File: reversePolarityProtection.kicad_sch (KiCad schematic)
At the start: 4 parts, among them Q7 XPH3R114MC

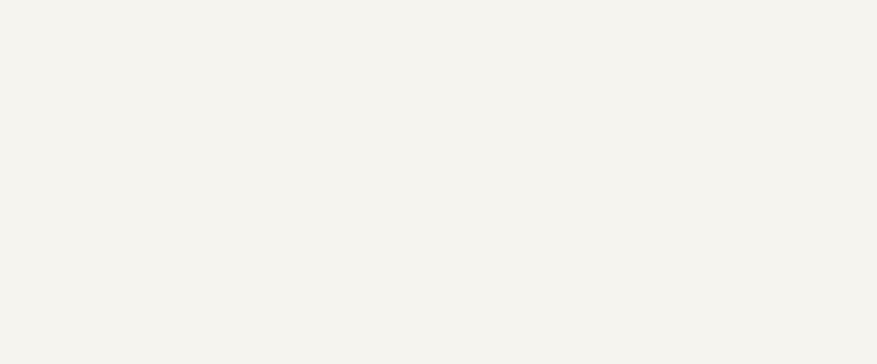
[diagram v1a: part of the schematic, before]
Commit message: Added Wakeup, supply, more pins on MCU
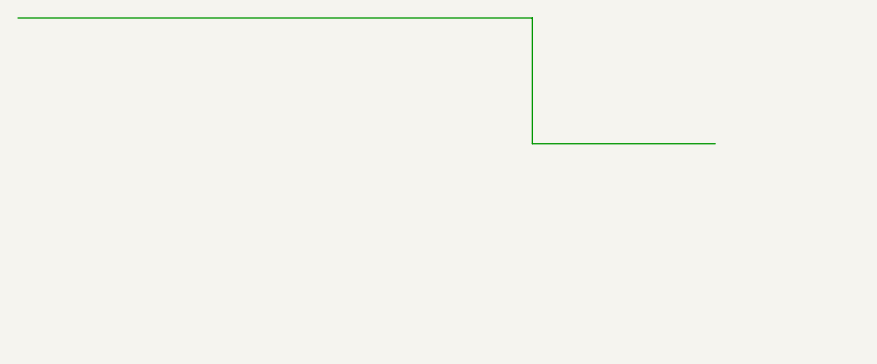
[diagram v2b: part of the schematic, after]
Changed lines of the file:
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@@
+	(wire
+		(pts
+			(xy 77.5462 14.0462) (xy 57.2262 14.0462)
+		)
+		(stroke
+			(width 0)
+			(type default)
+		)
+	)
 	(wire
 		(pts
@@
 	(wire
 		(pts
+			(xy 57.2262 14.0462) (xy 57.2262 0.0762)
+		)
+		(stroke
+			(width 0)
+			(type default)
+		)
+	)
+	(wire
+		(pts
 			(xy 154.94 90.17) (xy 154.94 96.52)
 		)
 		(stroke
+			(width 0)
+			(type default)
+		)
+	)
+	(wire
+		(pts
+			(xy 57.2262 0.0762) (xy 0.0762 0.0762)
+		)
+		(stroke

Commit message: Checked pinouts
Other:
- note added: "Checked ok"
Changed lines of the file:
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@@
 	(generator_version "10.0")
 	(paper "A4")
+	(text "Checked ok"
+		(exclude_from_sim no)
+		(at 199.39 173.482 0)
+		(effects
+			(font
+				(size 1.27 1.27)
+			)
+		)
+	)
 	(junction
 		(at 162.56 82.55)

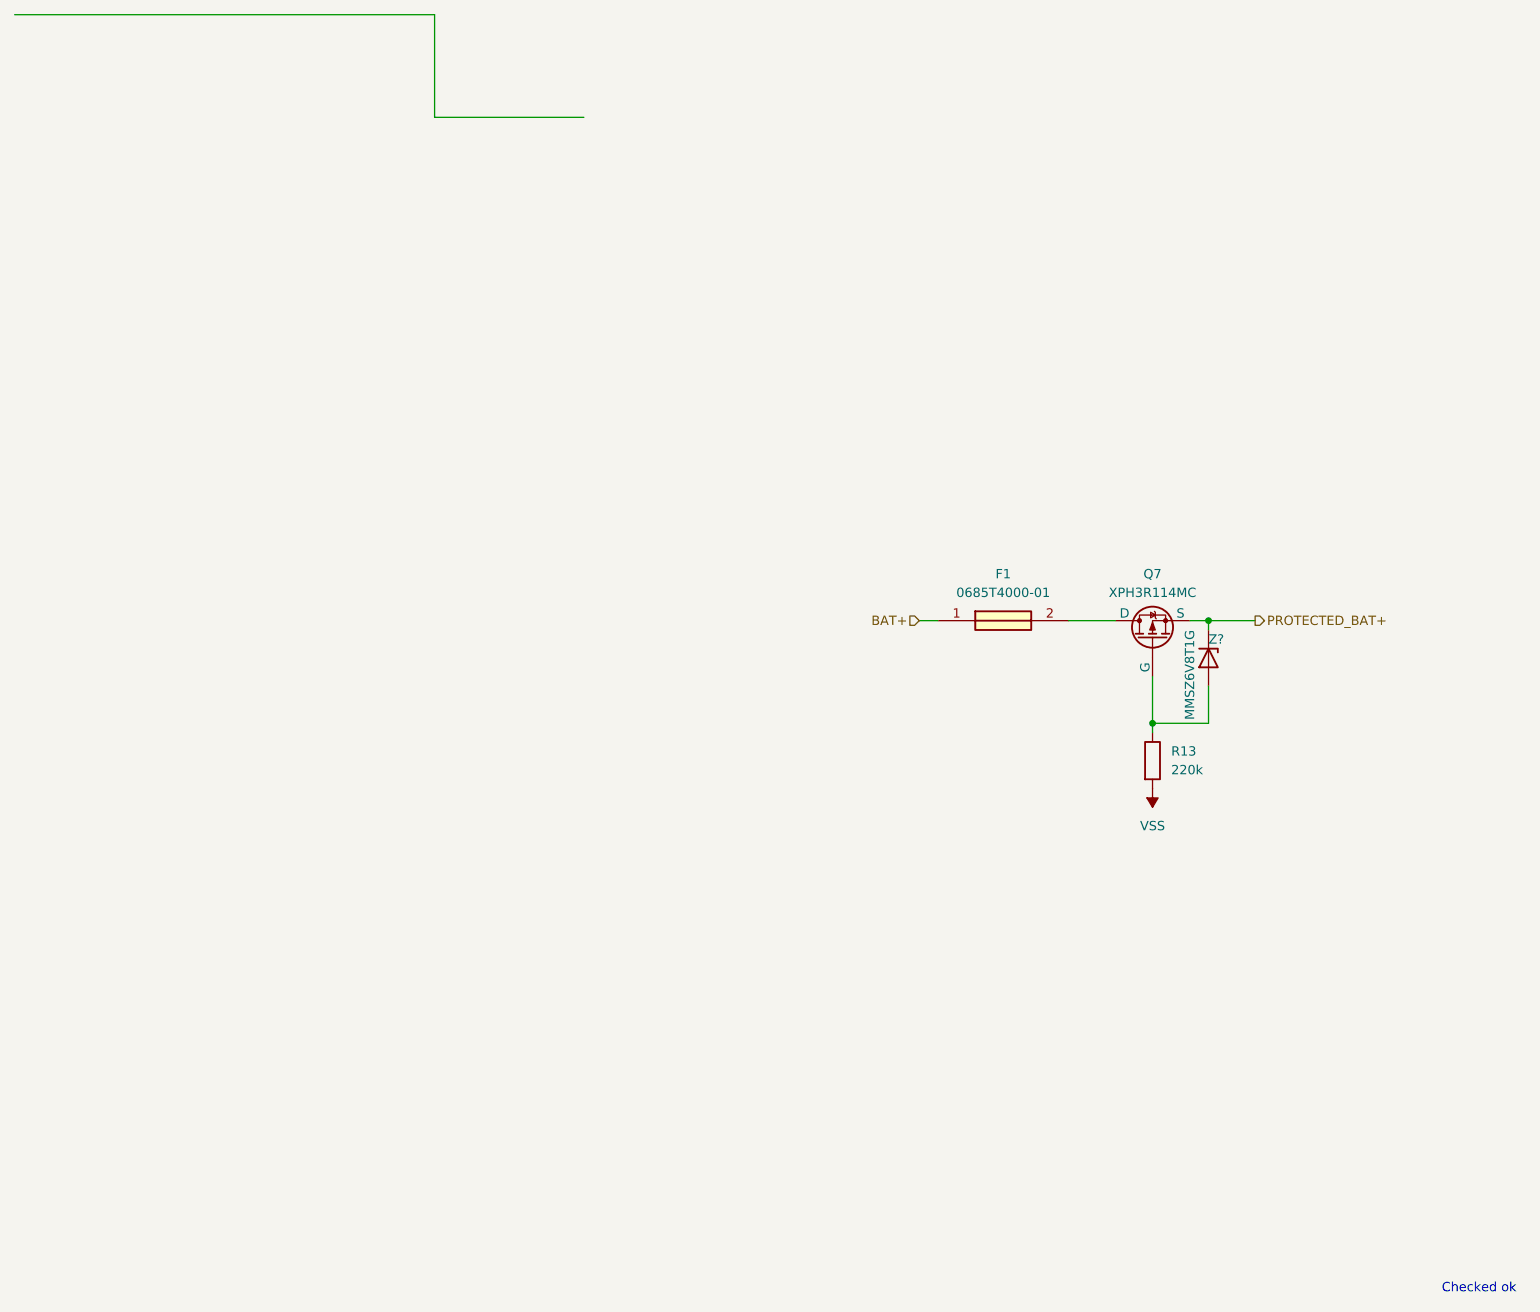
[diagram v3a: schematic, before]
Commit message: Review and update reversePolarityProtection schematic
- Annotate Zener Z? → Z1
- Replace fuse F1: 0685T4000-01 (4A Bel) → SF-1206HH25M-2 (25A Bourns),
  same 1206 footprint updated to Fuse:Fuse_1206_3216Metric
- Add TVS1 TPSMF4L20A (Littelfuse SOD-123FL, 20V standoff, 32.4V clamp,
  AEC-Q101) on BAT+ input rail for ISO 7637-2 load dump protection
- Add C1 4.7uF/50V X7R MLCC 1210 (Murata GRM32ER71H475KA88L) in parallel
  with TVS1 for high-frequency transient bypass, zero leakage in sleep
- Fix Q7 (XPH3R114MC) datasheet link: was ngspice URL, now Toshiba datasheet
- Remove three orphaned stray wires near schematic origin (0,0)

https://claude.ai/code/session_01Q9peTQ2YtBwmEgSRVprrxD
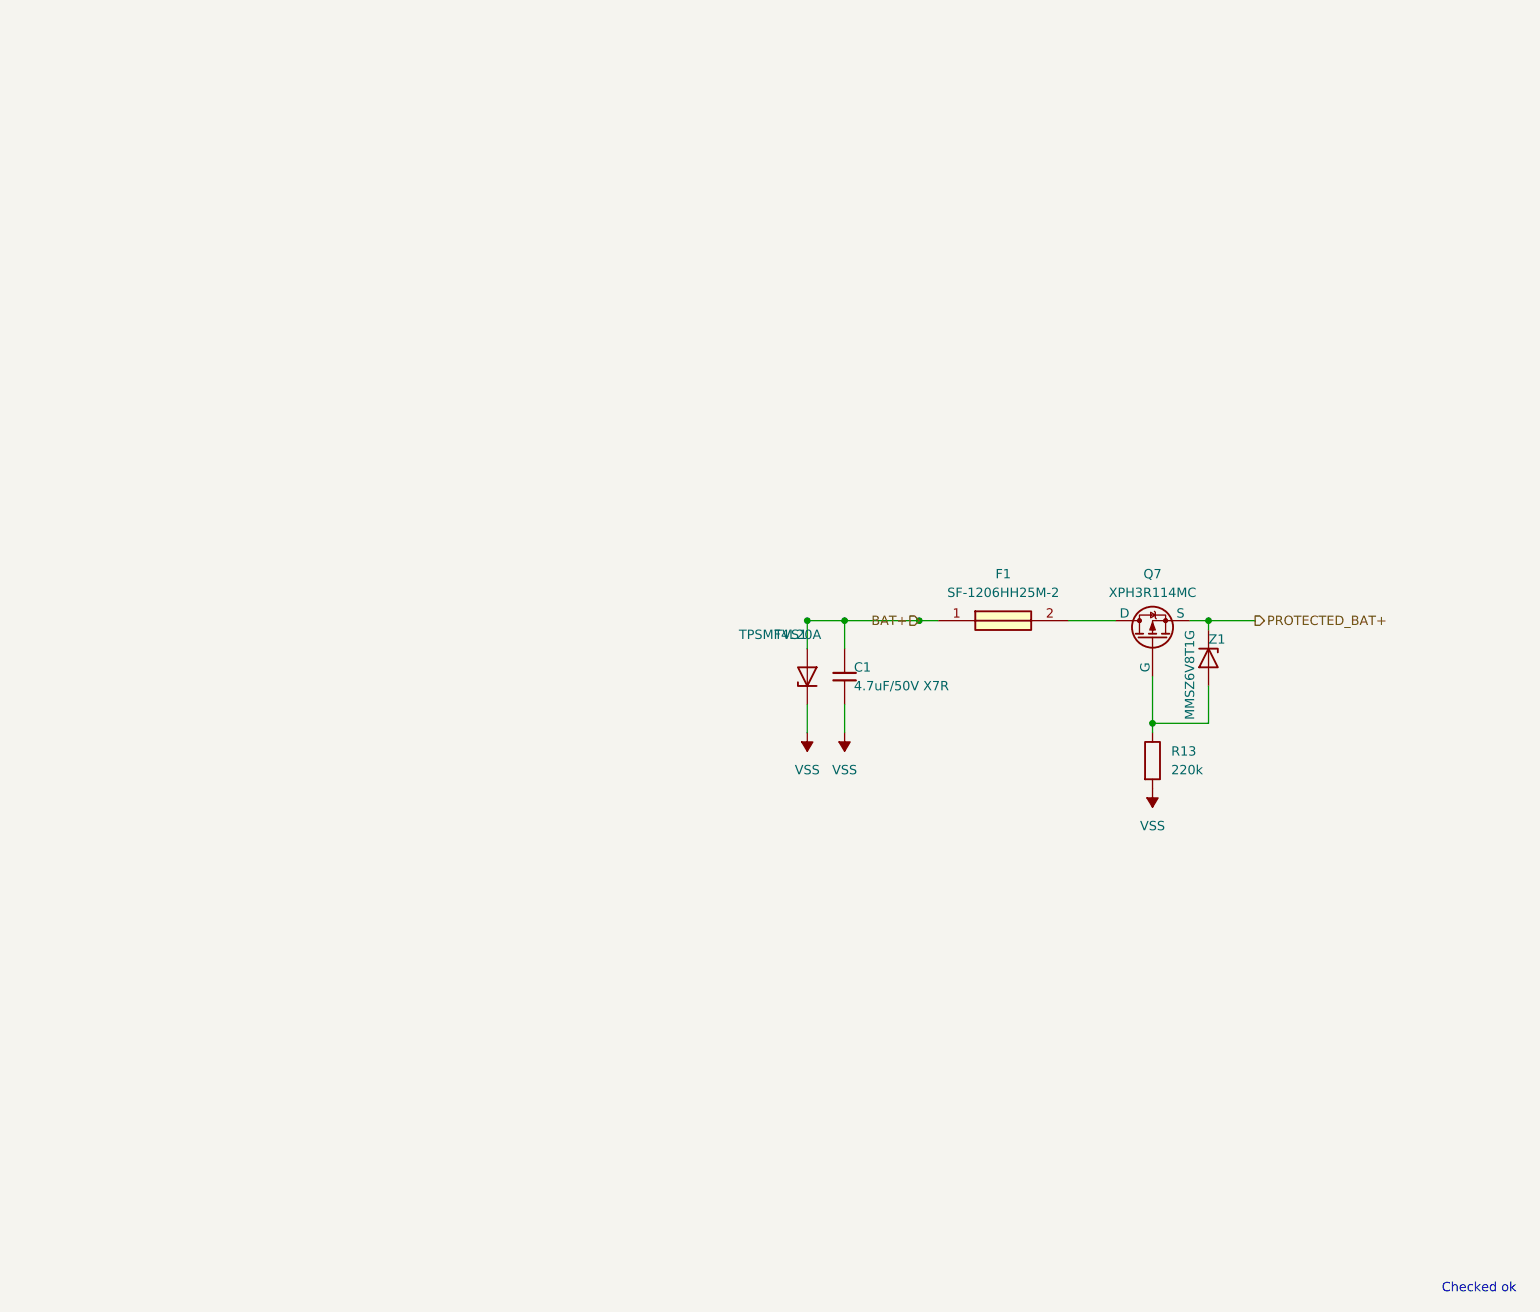
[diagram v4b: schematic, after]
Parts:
- added C1: 4.7uF/50V X7R, Capacitor_SMD:C_1210_3225Metric, symbol Device:C
- added TVS1: TPSMF4L20A, Diode_SMD:D_SOD-123FL, symbol Device:D_Zener
- F1: value 0685T4000-01 -> SF-1206HH25M-2; footprint FUSC3216X83N -> Fuse:Fuse_1206_3216Metric; symbol SamacSys_Parts:0685T4000-01 -> SamacSys_Parts:SF-1206HH25M-2; Manufacturer_Name Bel Circuit Protection -> Bourns; Manufacturer_Part_Number 0685T4000-01 -> SF-1206HH25M-2
- gave numbers to parts that had none: 1
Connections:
- net BAT+: now also C1.1, TVS1.2 (A)
- net VSS: now also C1.2, TVS1.1 (K)
